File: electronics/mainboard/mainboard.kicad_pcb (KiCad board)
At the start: 2 copper layers, 43.7 x 137 mm, 24 parts, among them Q1 TSM250N02CX_RFG, Q2 TSM250N02CX_RFG, SW1 SW_Push, SW10 SW_Push, SW11 SW_Push, SW12 SW_Push, SW13 SW_Push, SW14 SW_Push, SW15 SW_Push, SW2 SW_Push, SW3 SW_Push, SW4 SW_Push, SW5 SW_Push, SW6 SW_Push, SW7 SW_Push, SW8 SW_Push, SW9 SW_Push, U1 1022

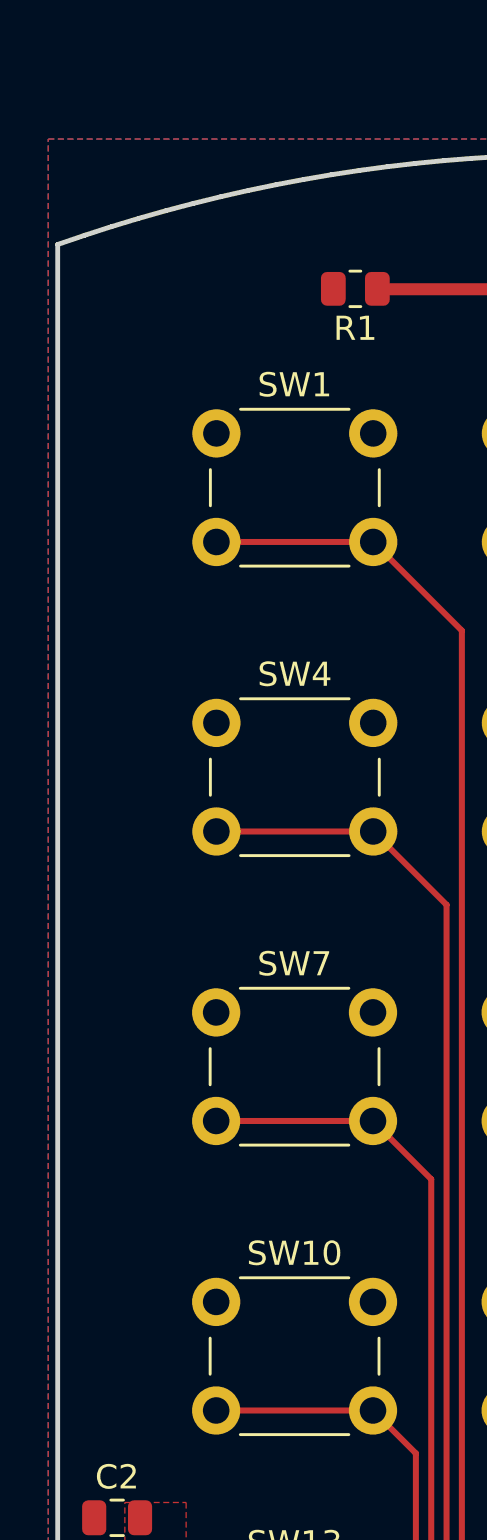
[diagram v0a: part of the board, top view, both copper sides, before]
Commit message: integrate workflow for automatic mainboard production data creation and releases
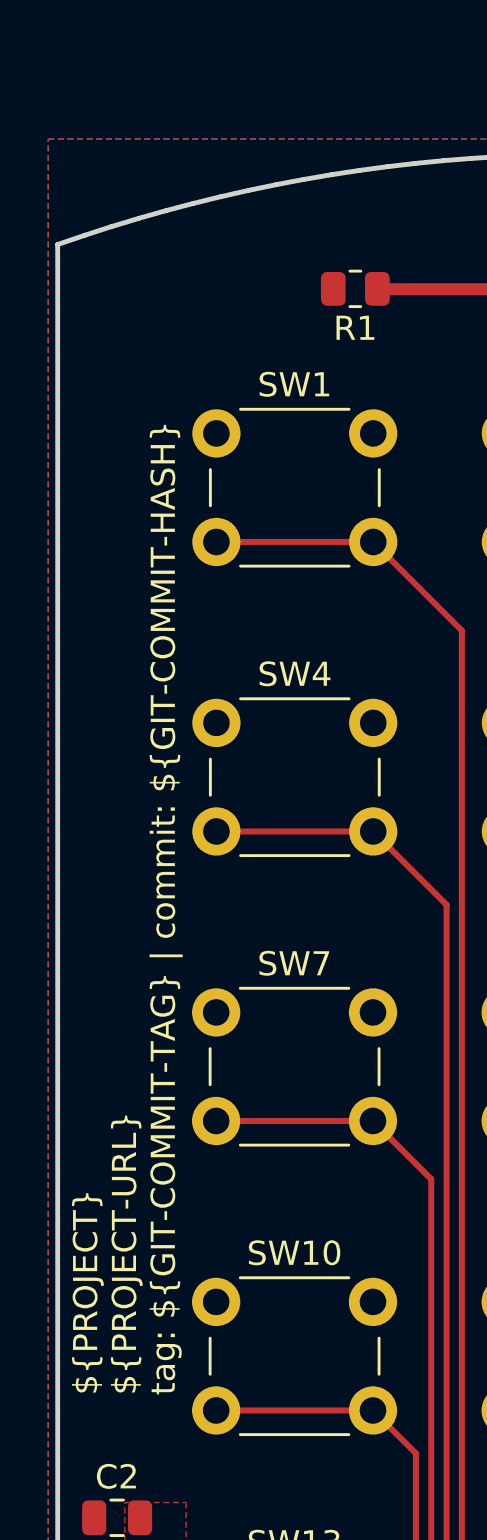
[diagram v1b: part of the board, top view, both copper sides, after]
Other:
- board text added: "${PROJECT} ${PROJECT-URL} tag: ${GIT-COMMIT-TAG} | commit: ${GIT-COMMIT-HASH}"
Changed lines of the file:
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@@
   )
   (paper "A4")
+  (title_block
+    (title "Mainboard")
+    (comment 1 "${PROJECT}")
+    (comment 2 "${PROJECT-URL}")
+    (comment 3 "${GIT-COMMIT-HASH}")
+    (comment 4 "${GIT-COMMIT-TAG}")
+  )
   (layers
     (0 "F.Cu" signal)
@@
   )
   (setup
+    (stackup
+      (layer "F.SilkS" (type "Top Silk Screen"))
+      (layer "F.Paste" (type "Top Solder Paste"))
+      (layer "F.Mask" (type "Top Solder Mask") (thickness 0.01))
+      (layer "F.Cu" (type "copper") (thickness 0.035))
+      (layer "dielectric 1" (type "core") (thickness 1.51) (material "FR4") (epsilon_r 4.5) (loss_tangent 0.02))
+      (layer "B.Cu" (type "copper") (thickness 0.035))
+      (layer "B.Mask" (type "Bottom Solder Mask") (thickness 0.01))
+      (layer "B.Paste" (type "Bottom Solder Paste"))
+      (layer "B.SilkS" (type "Bottom Silk Screen"))
+      (copper_finish "None")
+      (dielectric_constraints no)
+    )
     (pad_to_mask_clearance 0)
     (grid_origin 110.2471 44.0637)
@@
     )
   )
+  (property "GIT-COMMIT-HASH" "noHash")
+  (property "GIT-COMMIT-TAG" "noTag")
+  (property "PROJECT" "Remote Control - Mainboard")
+  (property "PROJECT-URL" "https://github.com/erichstuder/RemoteControl")
   (net 0 "")
   (net 1 "unconnected-(A1-Pad3)")
@@
   (gr_line (start 121.3867 122.2996) (end 121.3654 122.2844) (layer "Edge.Cuts") (width 0.2))
   (gr_line (start 122.2994 119.5718) (end 122.3256 119.57294) (layer "Edge.Cuts") (width 0.2))
+  (gr_text "${PROJECT}\n${PROJECT-URL}\ntag: ${GIT-COMMIT-TAG} | commit: ${GIT-COMMIT-HASH}" (at 91.1971 95.4987 90) (layer "F.SilkS")
+    (effects (font (size 1 1) (thickness 0.15)) (justify left))
+  )
   (segment (start 101.67996 49.655) (end 108.9727 49.655) (width 0.5) (layer "F.Cu") (net 11))
   (segment (start 101.663509 49.638549) (end 101.67996 49.655) (width 0.25) (layer "F.Cu") (net 11))

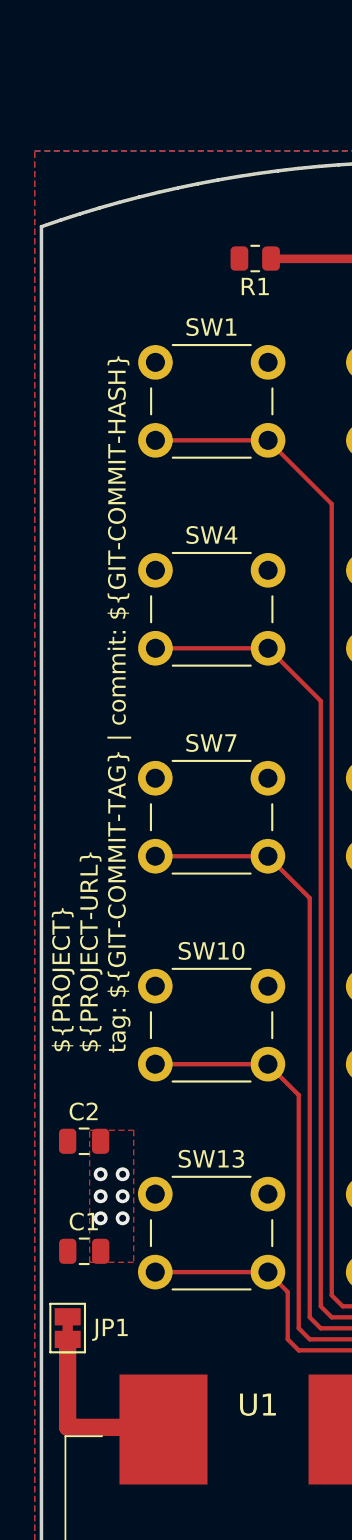
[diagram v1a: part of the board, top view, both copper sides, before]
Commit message: add a fuse
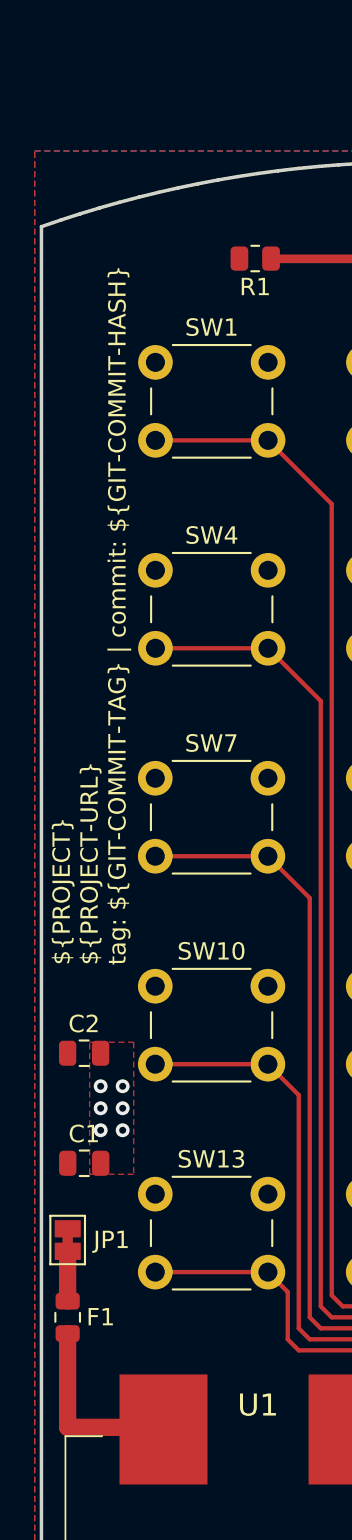
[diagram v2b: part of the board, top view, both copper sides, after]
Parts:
- added F1: Fuse 1A, Fuse:Fuse_0805_2012Metric, F.Cu at (89.9, 110.7)
- moved C1 5.08 mm to (90.9, 101.8)
- moved C2 5.08 mm to (90.9, 95.5)
- moved JP1 5.08 mm to (89.9, 106.3)
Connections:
- U1 pad 2: Net-(JP1-Pad1) -> Net-(U1-Pad2)
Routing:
- net Net-(U1-Pad2): track 0.00 -> 11.0 mm
- net Net-(JP1-Pad1): track 10.7 -> 2.87 mm
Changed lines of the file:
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@@
   (net 33 "unconnected-(A1-Pad19)")
   (net 34 "Net-(A1-Pad26)")
+  (net 35 "Net-(U1-Pad2)")
   (footprint "TSM250N02CX_RFG:TRANS_TSM250N02CX_RFG" (layer "F.Cu")
     (at 129.2971 129.1537 90)
@@
   )
   (footprint "Capacitor_SMD:C_0805_2012Metric" (layer "F.Cu")
-    (at 90.8771 100.5787)
+    (at 90.8771 95.4987)
     (descr "Capacitor SMD 0805 (2012 Metric), square (rectangular) end terminal, IPC_7351 nominal, (Body size source: IPC-SM-782 page 76, https://www.pcb-3d.com/wordpress/wp-content/uploads/ipc-sm-782a_amendment_1_and_2.pdf, https://docs.google.com/spreadsheets/d/1BsfQQcO9C6DZCsRaXUlFlo91Tg2WpOkGARC1WS5S8t0/edit?usp=sharing), generated with kicad-footprint-generator")
     (tags "capacitor")
@@
       (net 30 "Net-(Q1-Pad3)") (pinfunction "1") (pintype "passive"))
     (pad "2" smd rect (at -27.57 5.455) (size 5.08 6.35) (layers "F.Cu" "F.Paste" "F.Mask")
-      (net 32 "Net-(JP1-Pad1)") (pinfunction "2") (pintype "passive"))
+      (net 35 "Net-(U1-Pad2)") (pinfunction "2") (pintype "passive"))
     (pad "3" smd rect (at 27.57 5.455) (size 5.08 6.35) (layers "F.Cu" "F.Paste" "F.Mask")
       (net 29 "Net-(U1-Pad3)") (pinfunction "3") (pintype "passive"))
@@
   )
   (footprint "Capacitor_SMD:C_0805_2012Metric" (layer "F.Cu")
-    (at 90.8821 106.9287)
+    (at 90.8821 101.8487)
     (descr "Capacitor SMD 0805 (2012 Metric), square (rectangular) end terminal, IPC_7351 nominal, (Body size source: IPC-SM-782 page 76, https://www.pcb-3d.com/wordpress/wp-content/uploads/ipc-sm-782a_amendment_1_and_2.pdf, https://docs.google.com/spreadsheets/d/1BsfQQcO9C6DZCsRaXUlFlo91Tg2WpOkGARC1WS5S8t0/edit?usp=sharing), generated with kicad-footprint-generator")
     (tags "capacitor")
@@
   )
   (footprint "Jumper:SolderJumper-2_P1.3mm_Bridged_Pad1.0x1.5mm" (layer "F.Cu")
-    (at 89.9271 111.3587 90)
+    (at 89.9271 106.2787 90)
     (descr "SMD Solder Jumper, 1x1.5mm Pads, 0.3mm gap, bridged with 1 copper strip")
     (tags "net tie solder jumper bridged")
@@
     (model "${KICAD6_3DMODEL_DIR}/Connector_PinHeader_2.54mm.3dshapes/PinHeader_1x15_P2.54mm_Vertical.wrl"
       (offset (xyz 15.24 0 0))
+      (scale (xyz 1 1 1))
+      (rotate (xyz 0 0 0))
+    )
+  )
+  (footprint "Fuse:Fuse_0805_2012Metric" (layer "F.Cu")
+    (at 89.9271 110.7387 90)
+    (descr "Fuse SMD 0805 (2012 Metric), square (rectangular) end terminal, IPC_7351 nominal, (Body size source: https://docs.google.com/spreadsheets/d/1BsfQQcO9C6DZCsRaXUlFlo91Tg2WpOkGARC1WS5S8t0/edit?usp=sharing), generated with kicad-footprint-generator")
+    (tags "fuse")
+    (property "Sheetfile" "mainboard.kicad_sch")
+    (property "Sheetname" "")
+    (attr smd)
+    (fp_text reference "F1" (at 0 1.905 180) (layer "F.SilkS")
+      (effects (font (size 1 1) (thickness 0.15)))
+    )
+    (fp_text value "Fuse 1A" (at 0 1.65 90) (layer "F.Fab") hide
+      (effects (font (size 1 1) (thickness 0.15)))
+    )
+    (fp_text user "${REFERENCE}" (at 0 0 90) (layer "F.Fab")
+      (effects (font (size 0.5 0.5) (thickness 0.08)))
+    )
+    (fp_line (start -0.258578 0.71) (end 0.258578 0.71) (layer "F.SilkS") (width 0.12))
+    (fp_line (start -0.258578 -0.71) (end 0.258578 -0.71) (layer "F.SilkS") (width 0.12))
+    (fp_line (start 1.68 -0.95) (end 1.68 0.95) (layer "F.CrtYd") (width 0.05))
+    (fp_line (start -1.68 -0.95) (end 1.68 -0.95) (layer "F.CrtYd") (width 0.05))
+    (fp_line (start -1.68 0.95) (end -1.68 -0.95) (layer "F.CrtYd") (width 0.05))
+    (fp_line (start 1.68 0.95) (end -1.68 0.95) (layer "F.CrtYd") (width 0.05))
+    (fp_line (start -1 0.6) (end -1 -0.6) (layer "F.Fab") (width 0.1))
+    (fp_line (start 1 0.6) (end -1 0.6) (layer "F.Fab") (width 0.1))
+    (fp_line (start -1 -0.6) (end 1 -0.6) (layer "F.Fab") (width 0.1))
+    (fp_line (start 1 -0.6) (end 1 0.6) (layer "F.Fab") (width 0.1))
+    (pad "1" smd roundrect (at -0.9375 0 90) (size 0.975 1.4) (layers "F.Cu" "F.Paste" "F.Mask") (roundrect_rratio 0.25)
+      (net 35 "Net-(U1-Pad2)") (pintype "passive"))
+    (pad "2" smd roundrect (at 0.9375 0 90) (size 0.975 1.4) (layers "F.Cu" "F.Paste" "F.Mask") (roundrect_rratio 0.25)
+      (net 32 "Net-(JP1-Pad1)") (pintype "passive"))
+    (model "${KICAD6_3DMODEL_DIR}/Fuse.3dshapes/Fuse_0805_2012Metric.wrl"
+      (offset (xyz 0 0 0))
       (scale (xyz 1 1 1))
       (rotate (xyz 0 0 0))
@@
   (gr_line (start 121.3867 122.2996) (end 121.3654 122.2844) (layer "Edge.Cuts") (width 0.2))
   (gr_line (start 122.2994 119.5718) (end 122.3256 119.57294) (layer "Edge.Cuts") (width 0.2))
-  (gr_text "${PROJECT}\n${PROJECT-URL}\ntag: ${GIT-COMMIT-TAG} | commit: ${GIT-COMMIT-HASH}" (at 91.1971 95.4987 90) (layer "F.SilkS")
+  (gr_text "${PROJECT}\n${PROJECT-URL}\ntag: ${GIT-COMMIT-TAG} | commit: ${GIT-COMMIT-HASH}" (at 91.1971 90.4187 90) (layer "F.SilkS")
     (effects (font (size 1 1) (thickness 0.15)) (justify left))
   )
@@
   (segment (start 117.1426 130.4237) (end 116.5471 130.4237) (width 0.25) (layer "F.Cu") (net 15))
   (segment (start 129.346602 130.4237) (end 129.9771 130.4237) (width 0.25) (layer "F.Cu") (net 15))
-  (via (at 91.8321 103.7537) (size 0.8) (drill 0.4) (layers "F.Cu" "B.Cu") (net 15))
+  (via (at 91.8321 98.6737) (size 0.8) (drill 0.4) (layers "F.Cu" "B.Cu") (net 15))
   (via (at 129.346602 130.4237) (size 0.8) (drill 0.4) (layers "F.Cu" "B.Cu") (free) (net 15))
-  (via (at 91.8321 102.4837) (size 0.8) (drill 0.4) (layers "F.Cu" "B.Cu") (net 15))
+  (via (at 91.8321 97.4037) (size 0.8) (drill 0.4) (layers "F.Cu" "B.Cu") (net 15))
   (via (at 131.2021 130.4237) (size 0.8) (drill 0.4) (layers "F.Cu" "B.Cu") (free) (net 15))
-  (via (at 91.8321 105.0237) (size 0.8) (drill 0.4) (layers "F.Cu" "B.Cu") (net 15))
+  (via (at 91.8321 99.9437) (size 0.8) (drill 0.4) (layers "F.Cu" "B.Cu") (net 15))
   (via (at 115.376602 130.4237) (size 0.8) (drill 0.4) (layers "F.Cu" "B.Cu") (net 15))
-  (via (at 93.1021 105.0237) (size 0.8) (drill 0.4) (layers "F.Cu" "B.Cu") (net 15))
+  (via (at 93.1021 99.9437) (size 0.8) (drill 0.4) (layers "F.Cu" "B.Cu") (net 15))
   (via (at 117.1426 130.4237) (size 0.8) (drill 0.4) (layers "F.Cu" "B.Cu") (net 15))
-  (via (at 93.1021 102.4837) (size 0.8) (drill 0.4) (layers "F.Cu" "B.Cu") (net 15))
-  (via (at 93.1021 103.7537) (size 0.8) (drill 0.4) (layers "F.Cu" "B.Cu") (net 15))
+  (via (at 93.1021 97.4037) (size 0.8) (drill 0.4) (layers "F.Cu" "B.Cu") (net 15))
+  (via (at 93.1021 98.6737) (size 0.8) (drill 0.4) (layers "F.Cu" "B.Cu") (net 15))
   (segment (start 104.5321 75.1694) (end 104.5321 110.1037) (width 0.25) (layer "F.Cu") (net 17))
   (segment (start 101.4927 72.13) (end 104.5321 75.1694) (width 0.25) (layer "F.Cu") (net 17))
@@
   (segment (start 130.5671 55.4937) (end 124.7284 49.655) (width 0.5) (layer "F.Cu") (net 31))
   (segment (start 129.2971 113.9137) (end 130.5671 112.6437) (width 0.5) (layer "F.Cu") (net 31))
-  (segment (start 95.336389 117.0887) (end 89.9271 117.0887) (width 1) (layer "F.Cu") (net 32))
-  (segment (start 95.457689 117.21) (end 95.336389 117.0887) (width 0.25) (layer "F.Cu") (net 32))
-  (segment (start 89.9271 117.0887) (end 89.9271 112.0087) (width 1) (layer "F.Cu") (net 32))
+  (segment (start 89.9271 109.8012) (end 89.9271 106.9287) (width 1) (layer "F.Cu") (net 32))
   (segment (start 128.0271 132.6487) (end 128.3471 132.3287) (width 0.25) (layer "F.Cu") (net 34))
   (segment (start 128.3471 132.3287) (end 128.3471 130.1537) (width 0.25) (layer "F.Cu") (net 34))
   (segment (start 128.0271 144.225001) (end 128.0271 132.6487) (width 0.25) (layer "F.Cu") (net 34))
   (segment (start 129.852099 146.05) (end 128.0271 144.225001) (width 0.25) (layer "F.Cu") (net 34))
+  (segment (start 95.336389 117.0887) (end 89.9271 117.0887) (width 1) (layer "F.Cu") (net 35))
+  (segment (start 95.457689 117.21) (end 95.336389 117.0887) (width 0.25) (layer "F.Cu") (net 35))
+  (segment (start 89.9271 117.0887) (end 89.9271 111.6762) (width 1) (layer "F.Cu") (net 35))
   (zone (net 15) (net_name "GND") (layer "F.Cu") (hatch edge 0.508)
     (priority 1)
@@
     (polygon
       (pts
-        (xy 93.7371 107.5637)
-        (xy 91.1971 107.5637)
-        (xy 91.1971 99.9437)
-        (xy 93.7371 99.9437)
+        (xy 93.7371 102.4837)
+        (xy 91.1971 102.4837)
+        (xy 91.1971 94.8637)
+        (xy 93.7371 94.8637)
       )
     )
